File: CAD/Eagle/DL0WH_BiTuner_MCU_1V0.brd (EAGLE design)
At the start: 96.5 x 73 mm, 133 parts, among them Q0321 ABS07-32.768KHZ, U0101 STM32L476RXT_64PIN_LDO, U0601 MC33996, U0701 MC33996, U0801 MC33996, U0921 TS5A23166, U0951 OPA354, U1001 MAX232_SOIC16, U1101 MAX232_SOIC16, U1201 LM53603-Q1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

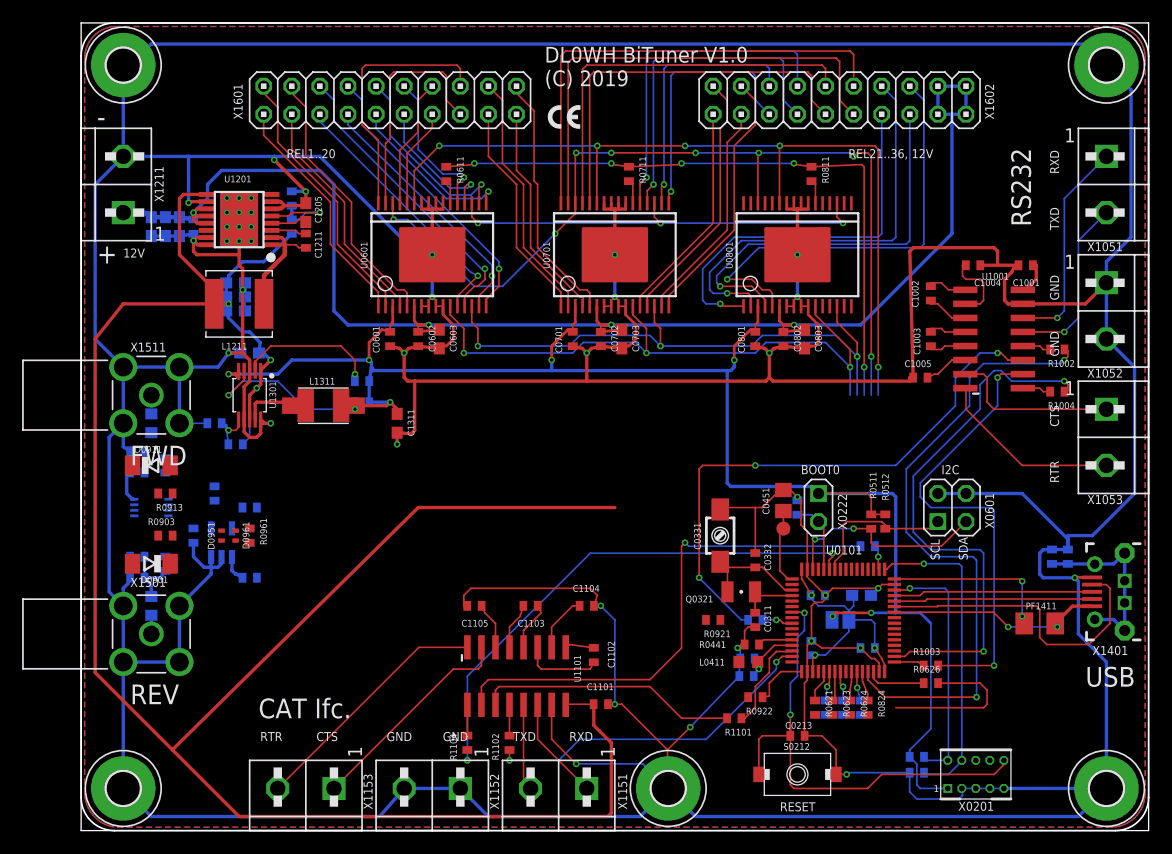
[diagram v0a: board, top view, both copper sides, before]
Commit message: HW_1V0 - CAD/Eagle - some parts re-routed
Signed-off-by: Ulrich Habel <espero7757@gmx.net>
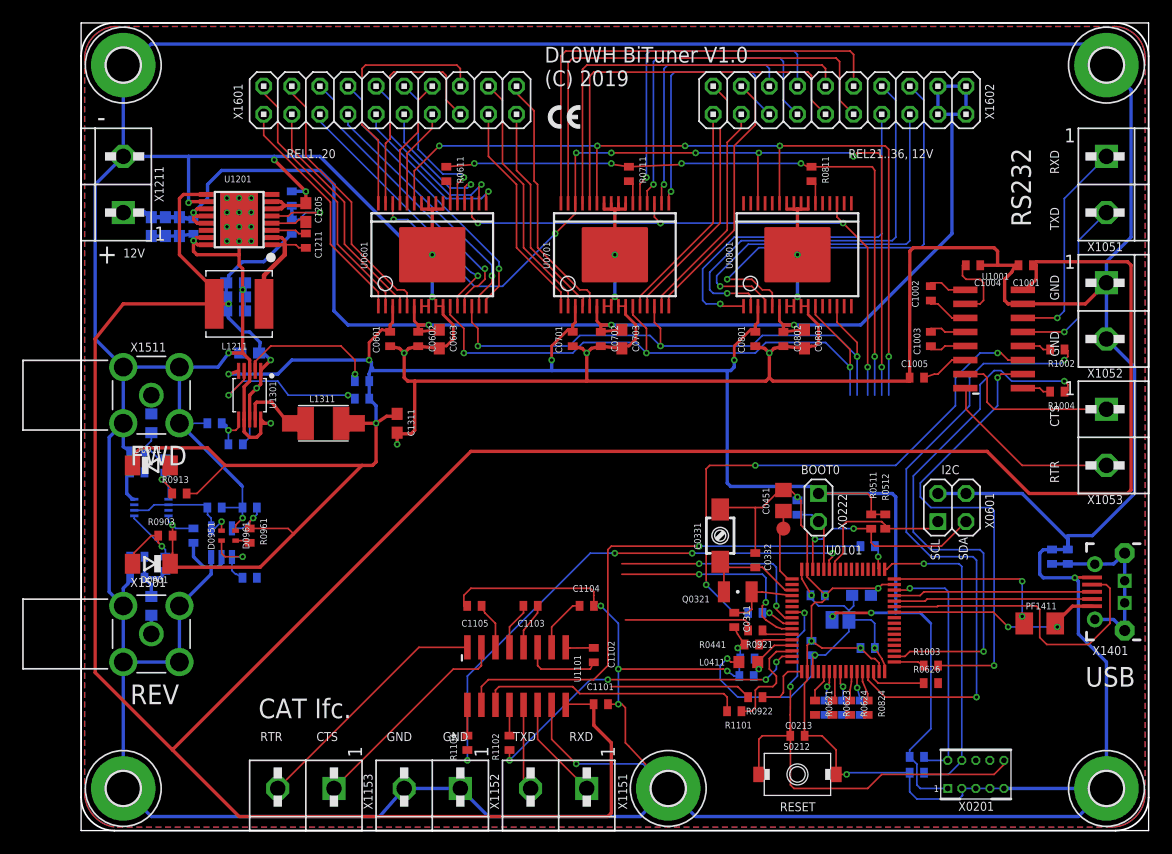
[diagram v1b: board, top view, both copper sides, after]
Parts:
- moved R0921 3.93 mm to (61.0, 18.1)
- moved C0311 1.91 mm to (59.1, 19.1)
- moved L1311 1.59 mm to (21.9, 36.8)
- moved R0913 1.27 mm to (8.89, 30.5), turned to 0 degrees
- moved R0951 1.27 mm to (12.1, 29.2), turned to 0 degrees
- moved R1101 0.63 mm to (59.1, 10.8)
- moved R1001 0.63 mm to (61.0, 19.7)
- moved R1321 0.32 mm to (25.4, 39.1)
- moved C1005 0.32 mm to (75.6, 41.0)
- moved Q0321 0.32 mm to (59.4, 21.6)
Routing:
- net +5V: track 204.2 -> 284.2 mm
- net +3V3: track 152.9 -> 220.5 mm, vias 7 -> 9
- net PC2: track 0.00 -> 21.2 mm, vias 0 -> 2
- net PC0: track 0.00 -> 19.6 mm, vias 0 -> 2
- net SPI_DRV_SI: track 39.1 -> 55.6 mm, vias 3 -> 4
- net GND: track 816.6 -> 831.7 mm, vias 29 -> 31
- net MCU_VDD: track 24.3 -> 39.2 mm, vias 3 -> 4
- net SPI_DRV_PWM: track 96.3 -> 82.9 mm
- net SWR_SEL_REV: track 0.00 -> 12.8 mm
- net SWR_SEL_FWD: track 0.00 -> 11.9 mm
- net SWR_SEL_PWR: track 0.00 -> 11.0 mm, vias 0 -> 1
- net SWR_IN_FWD: track 0.00 -> 9.80 mm, vias 0 -> 1
- net SWR_IN_REV: track 0.00 -> 6.03 mm, vias 0 -> 1
- net SWR_IN_REV_HI: track 0.00 -> 6.00 mm
- net SWR_OP_OUT: track 2.41 -> 6.56 mm, vias 0 -> 1
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
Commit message: HW_1V0 - CAD/Eagle - all placed, next: ERC and DRC
Signed-off-by: Ulrich Habel <espero7757@gmx.net>
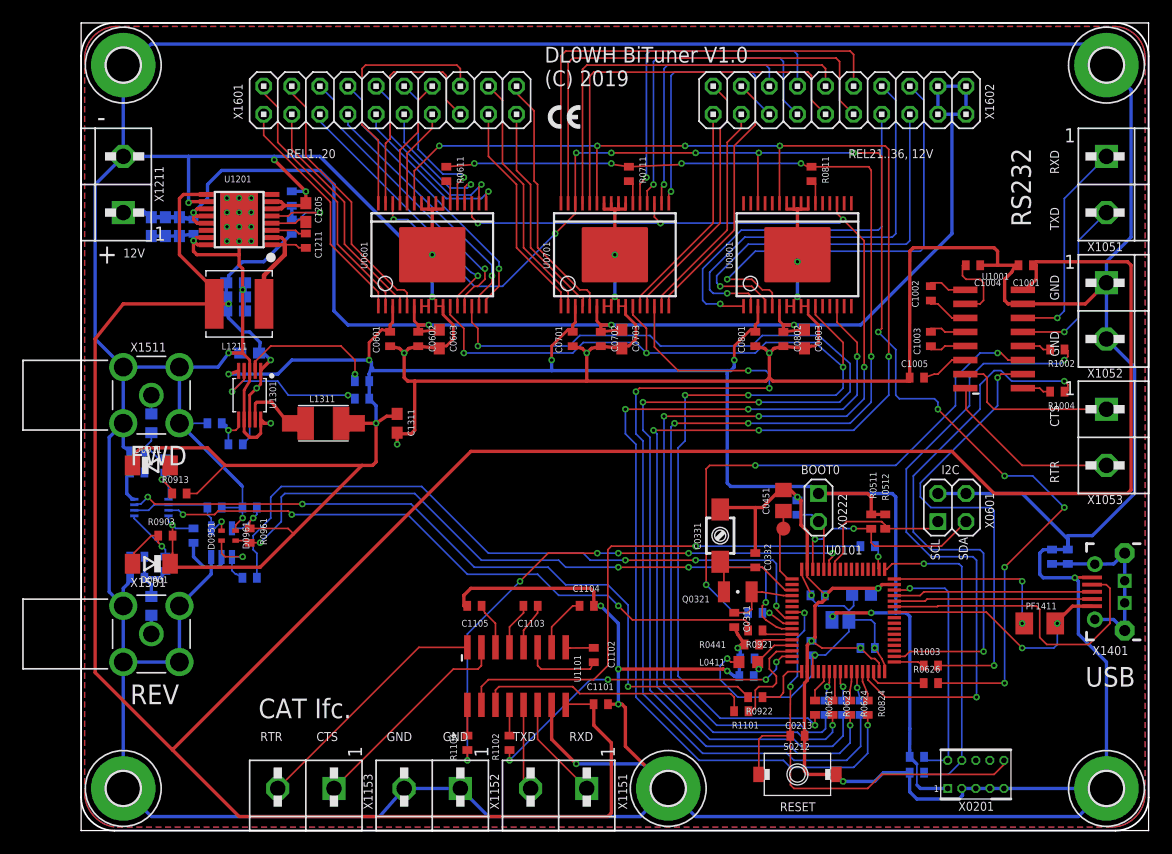
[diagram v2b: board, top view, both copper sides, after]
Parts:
- moved R1101 0.63 mm to (59.7, 10.8)
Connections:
- net SPI_DRV_C_!CS: now also U0701.14
- net SPI_DRV_EXT_!CS: now also U0801.14
- net SPI_DRV_L_!CS: no longer U0701.14, U0801.14
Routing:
- net SPI_DRV_EXT_!CS: track 0.00 -> 84.3 mm, vias 0 -> 4
- net SPI_DRV_C_!CS: track 0.00 -> 81.7 mm, vias 0 -> 3
- net SPI_DRV_!RST: track 79.5 -> 146.8 mm, vias 5 -> 7
- net SPI_DRV_SI: track 55.6 -> 117.9 mm, vias 4 -> 7
- net SPI_DRV_SO: track 59.5 -> 119.0 mm, vias 5 -> 7
- net SPI_DRV_L_!CS: track 52.7 -> 111.0 mm, vias 3 -> 4
- net SWR_SEL_REV: track 12.8 -> 67.6 mm, vias 0 -> 3
- net SPI_DRV_SCLK: track 55.9 -> 109.6 mm, vias 3 -> 6
- net SWR_SEL_FWD: track 11.9 -> 57.6 mm, vias 0 -> 3
- net SPI_DRV_PWM: track 82.9 -> 127.4 mm, vias 8 -> 13
- net PC0: track 19.6 -> 63.0 mm, vias 2 -> 3
- net PC2: track 21.2 -> 61.4 mm, vias 2 -> 4
- net PB7: track 46.8 -> 50.0 mm, vias 4 -> 6
- net +3V3: track 220.5 -> 218.2 mm
- net PA9: track 20.4 -> 22.4 mm
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
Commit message: HW_1V0 - CAD/Eagle - some DRC error fixed
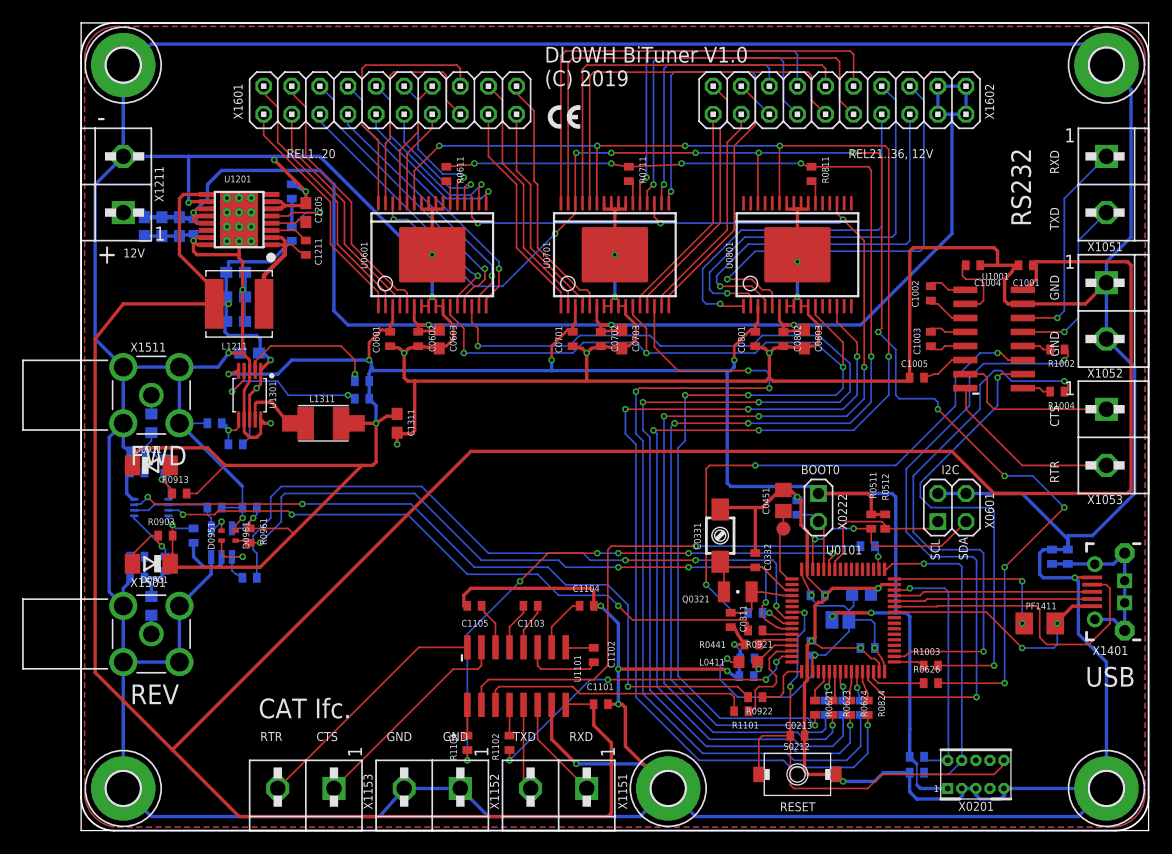
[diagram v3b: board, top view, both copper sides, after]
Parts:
- moved C1221 0.95 mm to (14.0, 50.5)
- moved C1223 0.95 mm to (14.0, 46.0)
- moved C1211 0.64 mm to (20.3, 52.7)
- moved C1201 0.63 mm to (5.71, 54.6)
- moved C1212 0.63 mm to (19.1, 57.8)
- moved R1211 0.63 mm to (19.1, 54.0)
- moved C0311 0.32 mm to (58.7, 19.1)
- moved C1202 0.32 mm to (7.30, 54.6)
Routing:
- net GND: track 832.7 -> 838.8 mm
- net +5V: track 284.5 -> 286.2 mm
- net LM53603_BIAS: track 8.57 -> 10.1 mm
- removed copper zone on layer 15, net +3V3
- removed copper zone on layer 2, net GND
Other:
- board text removed: "3x 2.8 mm"
- board text removed: "poly <--> edge: 12.5 mil socket <--> edge: 50.0 mil"

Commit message: HW_1V0 - CAD/Eagle - I/O protection on V24 lines added
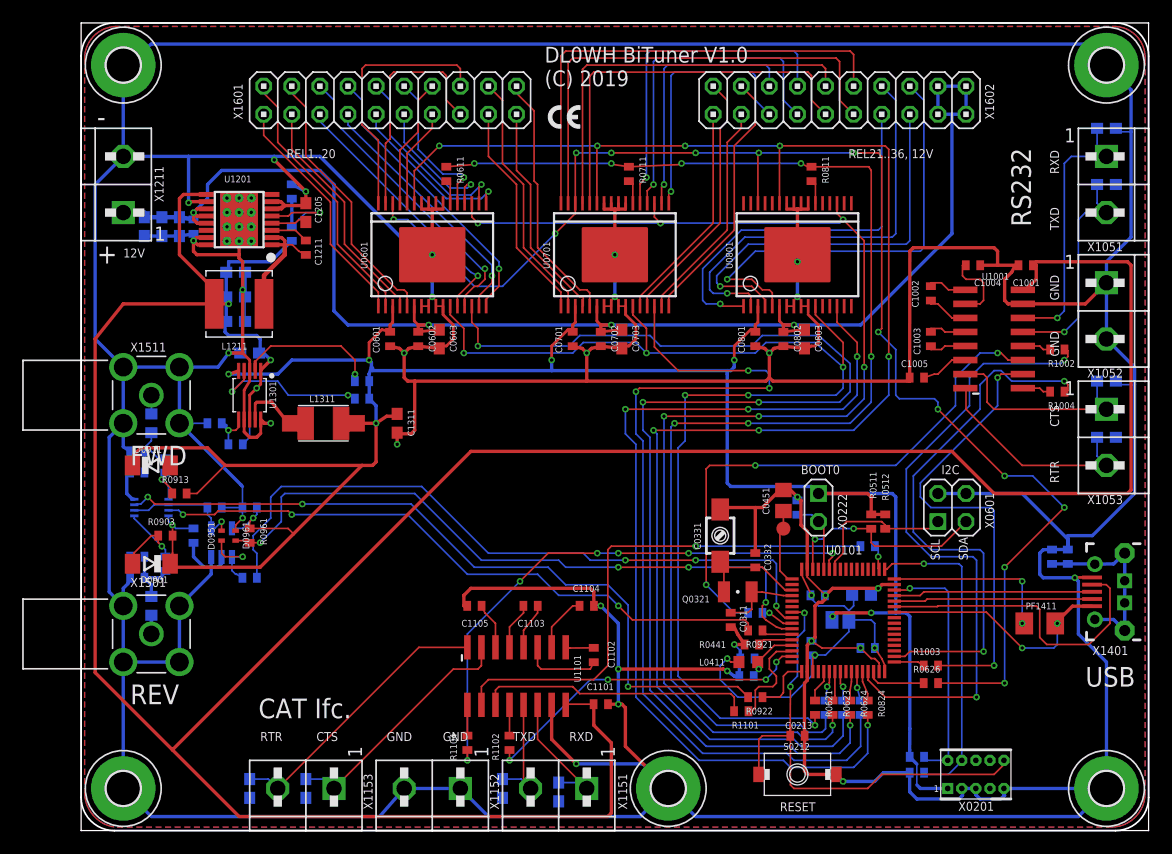
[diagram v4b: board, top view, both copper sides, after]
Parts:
- added C0054, C1051, C1052, C1053, C1151, C1152, C1153, C1154: 10nF, df4iah_rcl:C0603
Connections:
- net CAT_DTE_CTS: now also C1153.1
- net CAT_DTE_RTR: now also C1154.1
- net CAT_DTE_RXD: now also C1151.1
- net CAT_DTE_TXD: now also C1152.1
- net GND: now also C0054.2, C1051.2, C1052.2, C1053.2, C1151.2, C1152.2, C1153.2, C1154.2
- net RS_DTE_CTS: now also C1053.1
- net RS_DTE_RTR: now also C0054.1
- net RS_DTE_RXD: now also C1051.1
- net RS_DTE_TXD: now also C1052.1
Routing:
- net GND: track 838.8 -> 851.6 mm
- net RS_DTE_RXD: track 19.6 -> 24.3 mm
- net RS_DTE_TXD: track 16.1 -> 20.1 mm
- net CAT_DTE_RTR: track 22.4 -> 25.3 mm
- net CAT_DTE_TXD: track 7.82 -> 10.7 mm
- net CAT_DTE_CTS: track 19.6 -> 22.5 mm
- net RS_DTE_RTR: track 16.7 -> 19.6 mm
- net RS_DTE_CTS: track 15.4 -> 18.3 mm
- net CAT_DTE_RXD: track 9.40 -> 12.2 mm

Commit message: HW_1V0 - CAD/Eagle - Final imporovements done. Ready for production.
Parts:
- moved TP_VBAT 0.63 mm to (63.5, 26.7)
- moved C0311 0.45 mm to (58.4, 18.7)
- moved R1102 0.32 mm to (38.7, 8.26)
- moved R1104 0.32 mm to (34.9, 8.26)
- moved C1151 0.32 mm to (43.2, 3.81)
- moved C1204 0.32 mm to (10.5, 54.6)
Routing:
- net GND: track 851.6 -> 852.3 mm
- net MCU_VBAT: track 6.94 -> 7.57 mm
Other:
- board text added: "1"
- board text added: "2"
- board text added: "21"
- board text added: "22"
- board text added: "23"
- board text added: "35"
- board text added: "36"
- board text added: "DL0WH BiTuner Ctrl V1.0 (C) 2019"
- board text added: "RELAY A"
- board text added: "RELAY B"
- board text removed: "DL0WH BiTuner V1.0 (C) 2019"
- board text removed: "REL1..20"
- board text removed: "REL21..36, 12V"
